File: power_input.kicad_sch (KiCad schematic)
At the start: 90 parts, among them J201 Conn_02x02_Odd_Even, J202 Conn_01x02, J203 Conn_01x02, J204 Conn_01x02, J205 Conn_01x02, J206 Conn_01x02, Q201 Q_PMOS_GSD, Q202 Q_NMOS_GSD, Q203 Q_PMOS_GSD, Q204 Q_PMOS_GSD, Q205 Q_PMOS_GSD, U201 LM397, U202 LM397, U203 LM321, U204 LM397

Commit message: Fix OCLO
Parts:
- removed Q205: Q_PMOS_GSD, symbol Transistor_FET:Q_PMOS_GSD
- removed R220: 1 k, symbol Device:R
- removed R225, R230: 100 k, symbol Device:R
- removed R228: 45 k, symbol Device:R
- added C217: 10 u, symbol Device:C
- added J202, J203, J208: Conn_01x02, symbol Connector_Generic:Conn_01x02
- added Q205: Q_NMOS_GSD, symbol Transistor_FET:Q_NMOS_GSD
- added Q206: Q_PMOS_GSD, symbol Transistor_FET:Q_PMOS_GSD
- added R229: 100 k, symbol Device:R
- added R232: 100, symbol Device:R
- added R233: 1 k, symbol Device:R
- added TP213, TP214: TestPoint, symbol Connector:TestPoint
- renumbered J202 to J204, J203 to J205, J204 to J206, J205 to J207, J206 to J209, R229 to R228, R231 to R230, R232 to R231
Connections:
- net GND: now also C217.2, Q205.2 (S)
- net OCLO_IN: now also R218.2, TP210.1, U203.4
- net OCLO_OUT_N: now also R232.1
- net V_IN_FILTERED: now also J202.1 (Pin_1), J203.1 (Pin_1)
- net V_IN_SHUNT: now also J208.1 (Pin_1), Q206.2 (S), R229.1
- net V_OCLO_OUT: now also J208.2 (Pin_2), Q206.3 (D)
- net V_OVLO_OUT: now also J203.2 (Pin_2)
- net V_UVLO_OUT: now also J202.2 (Pin_2)
- net at D211.2 (A): now also Q206.1 (G), R229.2, R233.1, TP214.1; no longer TP212.1
- new net: Q205.3 (D), R233.2, TP213.1
- new net: C217.1, Q205.1 (G), R232.2, TP212.1
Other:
- note removed: "R_{HYST1}"
- note removed: "R_{HYST2}"
- moved on the sheet: C212, C213, C214, C215, C216, D207, R206, R213, R214, R215, R216, R218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

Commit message: Reformat power input
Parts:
- removed D208: LED, symbol Device:LED
- removed J209: Conn_01x02, symbol Connector_Generic:Conn_01x02
- removed R221, R226: 0, symbol Device:R
- removed R231: 5.1 k, symbol Device:R
- removed TP210, TP211: TestPoint, symbol Connector:TestPoint
- added C218: 10 u, symbol Device:C_Polarized
- added D211: LED, symbol Device:LED
- added J207: Conn_01x02, symbol Connector_Generic:Conn_01x02
- added R225: 0, symbol Device:R
- added R228, R229: 5.1k, symbol Device:R
- added TP208, TP209: TestPoint, symbol Connector:TestPoint
- R222, R224: value 5.1 k -> 0
- R227: value 5.1 k -> 5.1k
- R230: value 0 -> 5.1k
- renumbered C213 to C206, C212 to C207, C214 to C208, C206 to C209, C208 to C210, C215 to C211, C210 to C212, C216 to C213, C211 to C214, C217 to C215, C207 to C216, C209 to C217, D207 to D205, D211 to D206, D205 to D207, D206 to D208, J208 to J203, J207 to J208, J203 to J209, Q205 to Q204, Q206 to Q205, Q204 to Q206, R213 to R209, R214 to R210, R215 to R211, R216 to R212, R218 to R213, R219 to R214, R229 to R215, R232 to R216, R209 to R217, R233 to R218, R210 to R219, R211 to R220, R212 to R221, R228 to R226, R217 to R231, TP212 to TP210, TP213 to TP211, TP214 to TP212, TP208 to TP213, TP209 to TP214, U203 to U202, U204 to U203, U202 to U204
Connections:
- net GND: now also C218.2, D211.1 (K)
- net OCLO_IN: now also TP208.1
- net OCLO_OUT_N: now also TP209.1
- net V_IN_FILTERED: now also C207.1, C208.1, C211.1, C213.1, R214.1, R222.1, U202.5 (V+), U203.5 (V+); no longer C201.1, C202.1, D204.1 (K), J202.1 (Pin_1), Q203.2 (S), R201.1, R202.1, R206.1, R209.1, R211.1, U201.5 (V+)
- net V_OCLO_OUT: now also C218.1, J207.1 (Pin_1), R225.1; no longer J206.1 (Pin_1)
- net V_OVLO_OUT: now also C201.1, C202.1, D204.1 (K), J202.1 (Pin_1), Q203.2 (S), R201.1, R202.1, R206.1, U201.5 (V+)
- net V_UVLO_OUT: now also J206.1 (Pin_1), R209.1, R211.1, R224.1; no longer R230.1
- net at R222.2: now also J204.2 (Pin_2), R227.1
- net at R230.2: now also D212.2 (A)
- net at J206.2 (Pin_2): now also R224.2, R229.1; no longer R227.1
- net at J205.2 (Pin_2), R223.2: now also R228.1; no longer R224.1
- net at D209.2 (A): now also R227.2; no longer R224.2
- net at D210.2 (A): now also R228.2; no longer R227.2
- removed net V_IN_SHUNT: C207.1, C208.1, C211.1, C213.1, D206.1 (K), J203.1 (Pin_1), Q205.2 (S), R211.2, R212.1, R214.1, R215.1, U202.5 (V+), U203.5 (V+)
- new net: J207.2 (Pin_2), R225.2, R230.1
- new net: D211.2 (A), R229.2
- new net V_IN_SHUNTED: D206.1 (K), J203.1 (Pin_1), Q205.2 (S), R211.2, R212.1, R215.1
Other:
- moved on the sheet: C201, C202, C206, C207, C208, C211, C213, C215, C216, C217, D201, D204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

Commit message: Fill BOM for power input sheet
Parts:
- removed C211: 4.7 u, symbol Device:C
- removed C212, C214: 560 u, symbol Device:C_Polarized
- removed C213: 0.1 u, symbol Device:C
- removed C215: 10 u, symbol Device:C
- removed C218: 10 u, symbol Device:C_Polarized
- removed R208, R212: 1 k, symbol Device:R
- removed R217: 5 k, symbol Device:R
- removed R221: 100 k, symbol Device:R
- removed R223, R225: 0, symbol Device:R
- removed R230: 5.1k, symbol Device:R
- added C210, C218: 10 µF, Capacitor_SMD:C_0603_1608Metric, symbol Device:C
- added C212: 4.7 µF, Capacitor_SMD:C_0603_1608Metric, symbol Device:C
- added C213, C215: 560 µF, Capacitor_THT:C_Radial_D5.0mm_H11.0mm_P2.00mm, symbol Device:C_Polarized
- added C214, C219: 0.1 µF, perfect_footprints:C_0402_1005Metric, symbol Device:C
- added R205, R222: 100 kΩ, perfect_footprints:R_0402_1005Metric, symbol Device:R
- added R209, R215, R218: 1 kΩ, Resistor_SMD:R_0603_1608Metric, symbol Device:R
- added R219: 100 Ω, perfect_footprints:R_0402_1005Metric, symbol Device:R
- added R227: 0 Ω, Resistor_SMD:R_0805_2012Metric, symbol Device:R
- added R231, R232, R233: 4.99 kΩ, perfect_footprints:R_0402_1005Metric, symbol Device:R
- C201: value 4.7 u -> 4.7 µF; footprint (none) -> Capacitor_SMD:C_0603_1608Metric; DigiKey Part Number (none) -> 490-7205-1-ND; MPN (none) -> GRM188R6YA475KE15D; Manufacturer (none) -> Murata Electronics; Voltage rating (none) -> ≥ 35 V
- C202: value 0.1 u -> 0.1 µF; footprint (none) -> perfect_footprints:C_0402_1005Metric; DigiKey Part Number (none) -> 490-10700-1-ND; MPN (none) -> GRM155R71H104KE14D; Manufacturer (none) -> Murata Electronics; Voltage rating (none) -> ≥ 35 V
- C203, C204: value 1 u -> 1 µF; footprint (none) -> Capacitor_SMD:C_0805_2012Metric; DigiKey Part Number (none) -> 1276-1029-1-ND; MPN (none) -> CL21B105KBFNNNE; Manufacturer (none) -> Samsung Electro-Mechanics; Voltage rating (none) -> ≥ 35 V
- C205: value 22 u -> 10 µF; footprint (none) -> Capacitor_SMD:C_0603_1608Metric; DigiKey Part Number (none) -> 490-13248-1-ND; MPN (none) -> GRM188R6YA106MA73D; Manufacturer (none) -> Murata Electronics; Voltage rating (none) -> ≥ 35 V
- C206: value 1000 p -> 1000 pF; footprint (none) -> perfect_footprints:C_0402_1005Metric; DigiKey Part Number (none) -> 490-GRM1555CYA103GE01DCT-ND; MPN (none) -> GRM1555CYA103GE01D; Manufacturer (none) -> Murata Electronics; Temperature Coefficient (none) -> C0G
- C207, C216: value 4.7 u -> 10 µF; footprint (none) -> Capacitor_SMD:C_0603_1608Metric; DigiKey Part Number (none) -> 490-13248-1-ND; MPN (none) -> GRM188R6YA106MA73D; Manufacturer (none) -> Murata Electronics; Voltage rating (none) -> ≥ 35 V
- C208, C217: value 0.1 u -> 4.7 µF; footprint (none) -> Capacitor_SMD:C_0603_1608Metric; DigiKey Part Number (none) -> 490-7205-1-ND; MPN (none) -> GRM188R6YA475KE15D; Manufacturer (none) -> Murata Electronics; Voltage rating (none) -> ≥ 35 V
- C209: value 10 u -> 0.1 µF; footprint (none) -> perfect_footprints:C_0402_1005Metric; DigiKey Part Number (none) -> 490-10700-1-ND; MPN (none) -> GRM155R71H104KE14D; Manufacturer (none) -> Murata Electronics; Voltage rating (none) -> ≥ 35 V
- C211: renamed from C210; value 560 u -> 560 µF; footprint (none) -> Capacitor_THT:C_Radial_D5.0mm_H11.0mm_P2.00mm; DigiKey Part Number (none) -> 732-8949-1-ND; MPN (none) -> 860020575015; Manufacturer (none) -> Würth Elektronik; Voltage rating (none) -> ≥ 35 V
- D201, D205: value D_Zener -> MM3Z5V1B; footprint (none) -> Diode_SMD:D_SMA; Breakdown voltage 5 V -> (none); DigiKey Part Number (none) -> MM3Z5V1BCT-ND; MPN (none) -> MM3Z5V1B; Manufacturer (none) -> onsemi; Zener voltage (none) -> 5 V
- D202: value D_TVS -> XCEZ30V,L3XHF; footprint (none) -> Diode_SMD:D_SOD-523; symbol Device:D_TVS -> Device:D_Zener; DigiKey Part Number (none) -> 264-XCEZ30VL3XHFCT-ND; MPN (none) -> XCEZ30V,L3XHF; Manufacturer (none) -> Toshiba Semiconductor and Storage
- D203, D204, D208: value D_Zener -> SMAZ16-13-F; footprint (none) -> Diode_SMD:D_SMA; Breakdown voltage 16 V -> (none); DigiKey Part Number (none) -> SMAZ16-FDICT-ND; MPN (none) -> SMAZ16-13-F; Manufacturer (none) -> Diodes Incorporated; Zener voltage (none) -> 16 V
- D206: value D_Zener -> MM3Z5V1B; footprint (none) -> Diode_SMD:D_SMA; Breakdown voltage 16 V -> (none); DigiKey Part Number (none) -> MM3Z5V1BCT-ND; MPN (none) -> MM3Z5V1B; Manufacturer (none) -> onsemi; Zener voltage (none) -> 5 V
- D207: value D_Zener -> SMAZ16-13-F; footprint (none) -> Diode_SMD:D_SMA; Breakdown voltage 5 V -> (none); DigiKey Part Number (none) -> SMAZ16-FDICT-ND; MPN (none) -> SMAZ16-13-F; Manufacturer (none) -> Diodes Incorporated; Zener voltage (none) -> 16 V
- D209, D210, D211, D212: value LED -> 150060RS75000; footprint (none) -> LED_SMD:LED_0603_1608Metric; DigiKey Part Number (none) -> 732-4978-1-ND; MPN (none) -> 150060RS75000; Manufacturer (none) -> Würth Elektronik
- F201: footprint (none) -> Fuse:Fuse_Bourns_MF-RHT200; DigiKey Part Number (none) -> 118-MF-RHT200/32-2CT-ND; MPN (none) -> MF-RHT200/32-2; Manufacturer (none) -> Bourns Inc.
- FL201: value Choke_CommonMode -> ACM7060-701-2PL-TL01; footprint (none) -> Inductor_SMD:L_CommonModeChoke_TDK_ACM7060; DigiKey Part Number (none) -> 445-2215-1-ND; MPN (none) -> ACM7060-701-2PL-TL01; Manufacturer (none) -> TDK Corporation
- J201: value Conn_02x02_Odd_Even -> Molex Mini-fit Jr; footprint (none) -> Connector_Molex:Molex_Mini-Fit_Jr_5569-08A2_2x04_P4.20mm_Horizontal; DigiKey Part Number (none) -> 0455860005-ND; MPN (none) -> 0455860005; Manufacturer (none) -> Molex
- J202, J203, J204, J205, J206, J207, J208, J209: value Conn_01x02 -> 61300211121; footprint (none) -> Connector_PinHeader_2.54mm:PinHeader_2x01_P2.54mm_Vertical; DigiKey Part Number (none) -> 732-5315-ND; MPN (none) -> 61300211121; Manufacturer (none) -> Würth Elektronik
- L201: footprint (none) -> Inductor_SMD:L_Vishay_IHLP-2020; DigiKey Part Number (none) -> 541-1085-1-ND; MPN (none) -> IHLP2020BZERR47M01; Manufacturer (none) -> Vishay Dale
- Q201, Q203, Q205, Q206: value Q_PMOS_GSD -> SQ2319CES; footprint (none) -> Package_TO_SOT_SMD:SOT-23; DigiKey Part Number (none) -> 742-SQ2319CES-T1_GE3CT-ND; MPN (none) -> SQ2319CES-T1_GE3; Manufacturer (none) -> Vishay Siliconix
- Q202, Q204: value Q_NMOS_GSD -> IRFL4315TRPBF; footprint (none) -> Package_TO_SOT_SMD:SOT-223; symbol Transistor_FET:Q_NMOS_GSD -> Transistor_FET:Q_NMOS_GDSD; DigiKey Part Number (none) -> IRFL4315TRPBFCT-ND; MPN (none) -> IRFL4315TRPBF; Manufacturer (none) -> Infineon Technologies
- R201: value 5 k -> 1 kΩ; footprint (none) -> Resistor_SMD:R_0603_1608Metric; DigiKey Part Number (none) -> 732-560112116014CT-ND; MPN (none) -> 560112116014; Manufacturer (none) -> Würth Elektronik; Tolerance (none) -> ± 1 %
- R202, R204: value 100 k -> 100 kΩ; footprint (none) -> perfect_footprints:R_0402_1005Metric; DigiKey Part Number (none) -> 732-560112110019CT-ND; MPN (none) -> 560112110019; Manufacturer (none) -> Würth Elektronik; Tolerance (none) -> ± 1 %
- R203: value 15 k -> 15 kΩ; footprint (none) -> perfect_footprints:R_0402_1005Metric; DigiKey Part Number (none) -> 732-560112110127CT-ND; MPN (none) -> 560112110127; Manufacturer (none) -> Würth Elektronik; Tolerance (none) -> ± 1 %
- R206: renamed from R205; value 10 k -> 10 kΩ; footprint (none) -> perfect_footprints:R_0402_1005Metric; DigiKey Part Number (none) -> 732-560112110020CT-ND; MPN (none) -> 560112110020; Manufacturer (none) -> Würth Elektronik
- R207: renamed from R206; value 100 k -> 100 kΩ; footprint (none) -> perfect_footprints:R_0402_1005Metric; DigiKey Part Number (none) -> 732-560112110019CT-ND; MPN (none) -> 560112110019; Manufacturer (none) -> Würth Elektronik
- R208: renamed from R207; value 100 -> 100 Ω; footprint (none) -> perfect_footprints:R_0402_1005Metric; DigiKey Part Number (none) -> 732-560112110022CT-ND; MPN (none) -> 560112110022; Manufacturer (none) -> Würth Elektronik
- R210: renamed from R209; value 1 k -> 1 kΩ; footprint (none) -> Resistor_SMD:R_0603_1608Metric; DigiKey Part Number (none) -> 732-560112116014CT-ND; MPN (none) -> 560112116014; Manufacturer (none) -> Würth Elektronik; Tolerance (none) -> ± 1 %
- R211: renamed from R210; value 50 k -> 50 kΩ; footprint (none) -> perfect_footprints:R_0402_1005Metric; DigiKey Part Number (none) -> 732-560112110136CT-ND; MPN (none) -> 560112110136; Manufacturer (none) -> Würth Elektronik; Tolerance (none) -> ± 1 %
- R212: renamed from R211; value 50 m -> 50 mΩ; footprint (none) -> Resistor_SMD:R_1206_3216Metric; DigiKey Part Number (none) -> 732-560050332001CT-ND; MPN (none) -> 560050332001; Manufacturer (none) -> Würth Elektronik; Power rating (none) -> ≥ 0.2 W; Tolerance (none) -> ± 1 %
- R213: value 50 k -> 1 kΩ; footprint (none) -> Resistor_SMD:R_0603_1608Metric; DigiKey Part Number (none) -> 732-560112116014CT-ND; MPN (none) -> 560112116014; Manufacturer (none) -> Würth Elektronik; Tolerance (none) -> ± 1 %
- R214: value 5 k -> 50 kΩ; footprint (none) -> perfect_footprints:R_0402_1005Metric; DigiKey Part Number (none) -> 732-560112110136CT-ND; MPN (none) -> 560112110136; Manufacturer (none) -> Würth Elektronik; Tolerance (none) -> ± 1 %
- R216: value 100 -> 100 kΩ; footprint (none) -> perfect_footprints:R_0402_1005Metric; DigiKey Part Number (none) -> 732-560112110019CT-ND; MPN (none) -> 560112110019; Manufacturer (none) -> Würth Elektronik
- R217: renamed from R215; value 100 k -> 100 kΩ; footprint (none) -> perfect_footprints:R_0402_1005Metric; DigiKey Part Number (none) -> 732-560112110019CT-ND; MPN (none) -> 560112110019; Manufacturer (none) -> Würth Elektronik
- R220: renamed from R219; value 390 k -> 390 kΩ; footprint (none) -> Resistor_SMD:R_0603_1608Metric; DigiKey Part Number (none) -> 732-560112116024CT-ND; MPN (none) -> 560112116024; Manufacturer (none) -> Würth Elektronik; Tolerance (none) -> ± 1 %
- R221: renamed from R220; value 33 k -> 33 kΩ; footprint (none) -> Resistor_SMD:R_0603_1608Metric; DigiKey Part Number (none) -> 732-560112116030CT-ND; MPN (none) -> 560112116030; Manufacturer (none) -> Würth Elektronik; Tolerance (none) -> ± 1 %
- R223: renamed from R218; value 1 k -> 1 kΩ; footprint (none) -> Resistor_SMD:R_0603_1608Metric; DigiKey Part Number (none) -> 732-560112116014CT-ND; MPN (none) -> 560112116014; Manufacturer (none) -> Würth Elektronik
- R224: value 0 -> 100 kΩ; footprint (none) -> perfect_footprints:R_0402_1005Metric; DigiKey Part Number (none) -> 732-560112110019CT-ND; MPN (none) -> 560112110019; Manufacturer (none) -> Würth Elektronik
- R225: renamed from R222; value 0 -> 0 Ω; footprint (none) -> Resistor_SMD:R_0805_2012Metric; DigiKey Part Number (none) -> 732-560112120002CT-ND; MPN (none) -> 560112120002; Manufacturer (none) -> Würth Elektronik
- R226: value 0 -> 0 Ω; footprint (none) -> Resistor_SMD:R_0805_2012Metric; DigiKey Part Number (none) -> 732-560112120002CT-ND; MPN (none) -> 560112120002; Manufacturer (none) -> Würth Elektronik
- R228, R229: value 5.1k -> 0 Ω; footprint (none) -> Resistor_SMD:R_0805_2012Metric; DigiKey Part Number (none) -> 732-560112120002CT-ND; MPN (none) -> 560112120002; Manufacturer (none) -> Würth Elektronik
- R230: renamed from R227; value 5.1k -> 4.99 kΩ; footprint (none) -> perfect_footprints:R_0402_1005Metric; DigiKey Part Number (none) -> 732-560112110247CT-ND; MPN (none) -> 560112110247; Manufacturer (none) -> Würth Elektronik
- R234: renamed from R231; value 100 k -> 100 kΩ; footprint (none) -> perfect_footprints:R_0402_1005Metric; DigiKey Part Number (none) -> 732-560112110019CT-ND; MPN (none) -> 560112110019; Manufacturer (none) -> Würth Elektronik
- TP201, TP202, TP203, TP204, TP205, TP206, TP207, TP208, TP209, TP210, TP211, TP212, TP213, TP214: footprint (none) -> TestPoint:TestPoint_Pad_D1.0mm
- U201, U203, U204: DigiKey Part Number (none) -> LM397MFX/NOPBCT-ND; MPN (none) -> LM397MFX/NOPB; Manufacturer (none) -> Texas Instruments
- U202: value LM321 -> OPA197; symbol Amplifier_Operational:LM321 -> Amplifier_Operational:OPA197xDBV; DigiKey Part Number (none) -> 296-47813-1-ND; MPN (none) -> OPA197IDBVR; Manufacturer (none) -> Texas Instruments
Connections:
- net CHASSIS: now also D202.2 (A); no longer D202.1 (A1)
- net GND: now also D206.2 (A), Q202.3 (S), Q204.3 (S), C210.2, C212.2, C213.2, C214.2, C215.2, C218.2, C219.2, R222.2; no longer D207.2 (A), Q202.2 (S), Q204.2 (S)
- net OCLO_IN: now also R214.2, U202.1; no longer R213.2, U202.4
- net OCLO_IN+: now also U202.3 (+); no longer U202.1 (+)
- net OCLO_IN-: now also R213.2, R214.1, U202.4 (-); no longer R213.1, U202.3 (-)
- net OCLO_OUT_N: now also R216.2, R219.1; no longer R216.1
- net OCLO_REF: now also R215.2; no longer R214.2
- net OVLO_IN: now also R222.1
- net OVLO_OUT_N: now also R224.2
- net OVLO_REF: now also D206.1 (K), R218.2; no longer D207.1 (K)
- net UVLO_OUT_N: now also R205.2
- net V_IN: now also R229.2; no longer R226.2
- net V_IN+: now also D202.1 (K); no longer D202.2 (A2)
- net V_IN_CM: now also C207.1
- net V_IN_FILTERED: now also R224.1, C210.1, C212.1, C213.1, C214.1, C215.1, C219.1, R215.1, R218.1; no longer C207.1, C216.1, R214.1
- net V_IN_SHUNTED: now also D207.1 (K), R213.1, R216.1; no longer D206.1 (K)
- net V_OCLO_OUT: now also R228.1, C218.1
- net V_OVLO_OUT: now also R229.1, R205.1
- net V_UVLO_OUT: now also R227.1; no longer R224.1
- net at Q205.1 (G), R217.2, R223.1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: now also D207.2 (A); no longer D206.2 (A)
- net at R228.2: now also J207.2 (Pin_2), R233.1; no longer D210.2 (A)
- net at R223.2, TP211.1: now also Q204.2 (D), Q204.4 (D); no longer Q204.3 (D)
- net at D204.2 (A), Q203.1 (G), R207.2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: now also R209.1
- net at D212.2 (A): now also R233.2
- net at Q204.1 (G), TP210.1: now also C216.1, R219.2; no longer R216.2
- net at TP206.1: now also Q202.2 (D), Q202.4 (D), R209.2; no longer Q202.3 (D)
- net at J205.2 (Pin_2): now also R226.2, R231.1; no longer R228.1
- net at D211.2 (A): now also R232.2; no longer R229.2
- new net: D210.2 (A), R231.2
- new net: J206.2 (Pin_2), R227.2, R232.1
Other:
- moved on the sheet: D204, D209, Q203, Q205, Q206, R202, R203, R208, R217, R220, R221, R223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

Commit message: Rework intro and power input sheets
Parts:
- removed D202: XCEZ30V,L3XHF, Diode_SMD:D_SOD-523, symbol Device:D_Zener
- removed J201: Molex Mini-fit Jr, Connector_Molex:Molex_Mini-Fit_Jr_5569-08A2_2x04_P4.20mm_Horizontal, symbol Connector_Generic:Conn_02x02_Odd_Even
- renumbered C208 to C207, C207 to C208, D203 to D202, D204 to D203, D205 to D204, D206 to D205, D207 to D206, D208 to D207, D209 to D208, D210 to D209, D211 to D210, D212 to D211, J202 to J201, J203 to J202, J204 to J203, J205 to J204, J206 to J205, J207 to J206, J208 to J207, J209 to J208, R206 to R205, R205 to R206
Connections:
- net V_IN_FILTERED: now also R216.1
- net V_IN_SHUNTED: no longer R216.1
- net V_IN renamed V_SYS
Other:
- moved on the sheet: C203, C204, C205, C208, C210, C213, C215, C217, C219, D202, D205, F201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

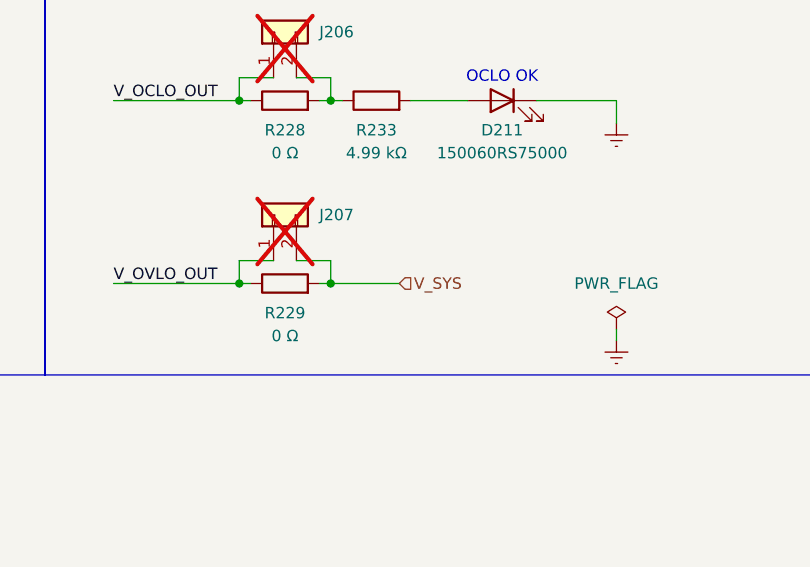
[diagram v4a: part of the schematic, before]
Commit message: Add power generation sheet
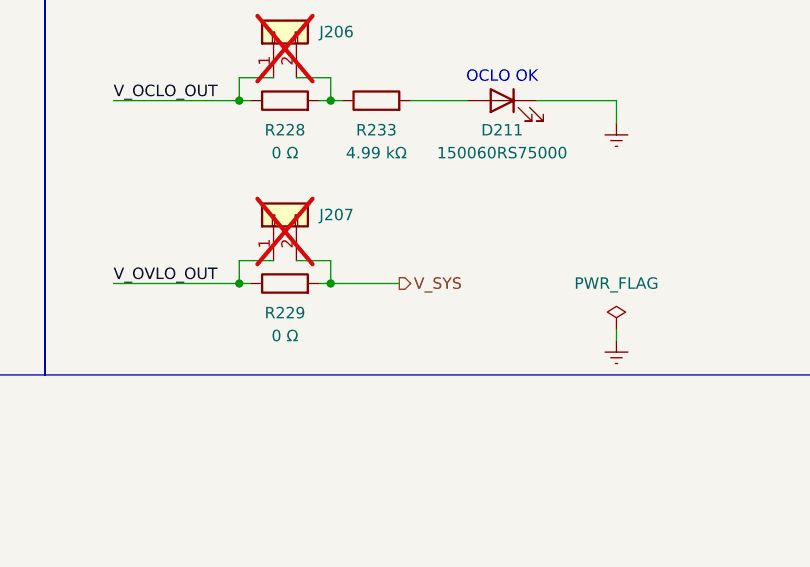
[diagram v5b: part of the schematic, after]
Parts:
- C206: Temperature Coefficient C0G -> (none); Temperature coefficient (none) -> C0G
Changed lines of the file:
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@@
 	)
 	(hierarchical_label "V_SYS"
-		(shape input)
+		(shape output)
 		(at 356.87 241.3 0)
 		(effects
@@
 			)
 		)
-		(property "Sim.Pins" ""
-			(at 139.7 88.9 0)
-			(effects
-				(font
-					(size 1.27 1.27)
-				)
-				(hide yes)
-			)
-		)
-		(property "Power" ""
-			(at 139.7 88.9 0)
-			(effects
-				(font
-					(size 1.27 1.27)
-				)
-				(hide yes)
-			)
-		)
 		(pin "2"
 		)
@@
 			)
 		)
-		(property "Temperature Coefficient" "C0G"
+		(property "Temperature coefficient" "C0G"
 			(at 171.45 215.9001 0)
 			(effects

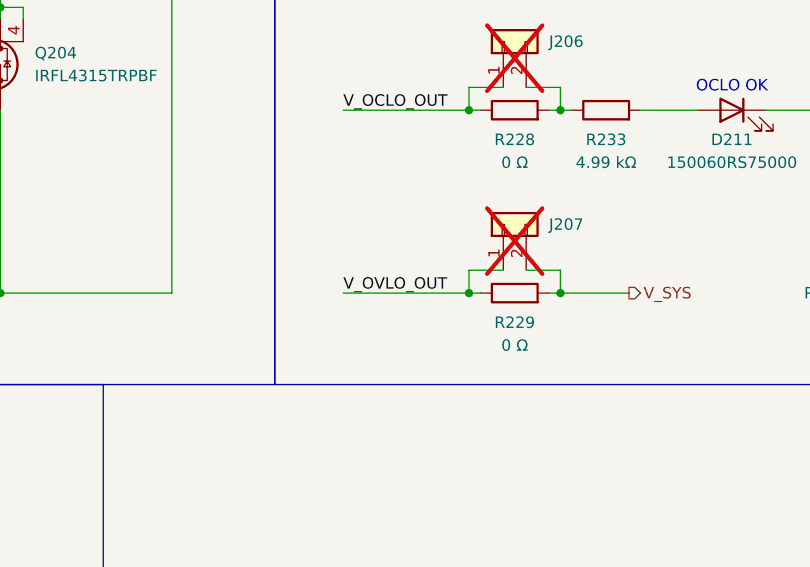
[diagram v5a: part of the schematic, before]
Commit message: Add 5V and 3.3V power generation
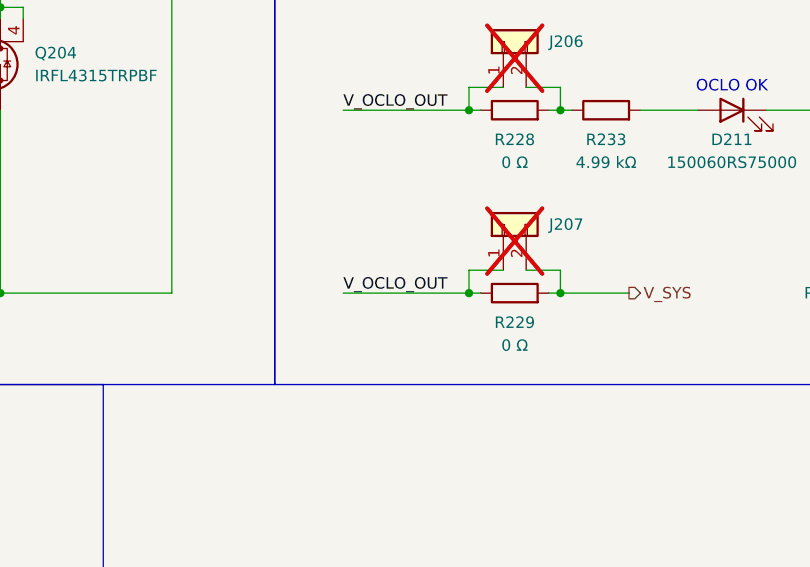
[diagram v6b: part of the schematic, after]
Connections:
- net V_OCLO_OUT: now also J207.1 (Pin_1), R229.1
- net V_OVLO_OUT: no longer J207.1 (Pin_1), R229.1
